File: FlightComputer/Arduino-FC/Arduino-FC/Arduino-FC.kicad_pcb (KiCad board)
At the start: 2 copper layers, 128.5 x 95.7 mm, 16 parts, among them J1 Conn_01x04, J2 Conn_01x08, J3 Conn_01x06, J4 Conn_01x03, J5 Conn_02x04_Odd_Even

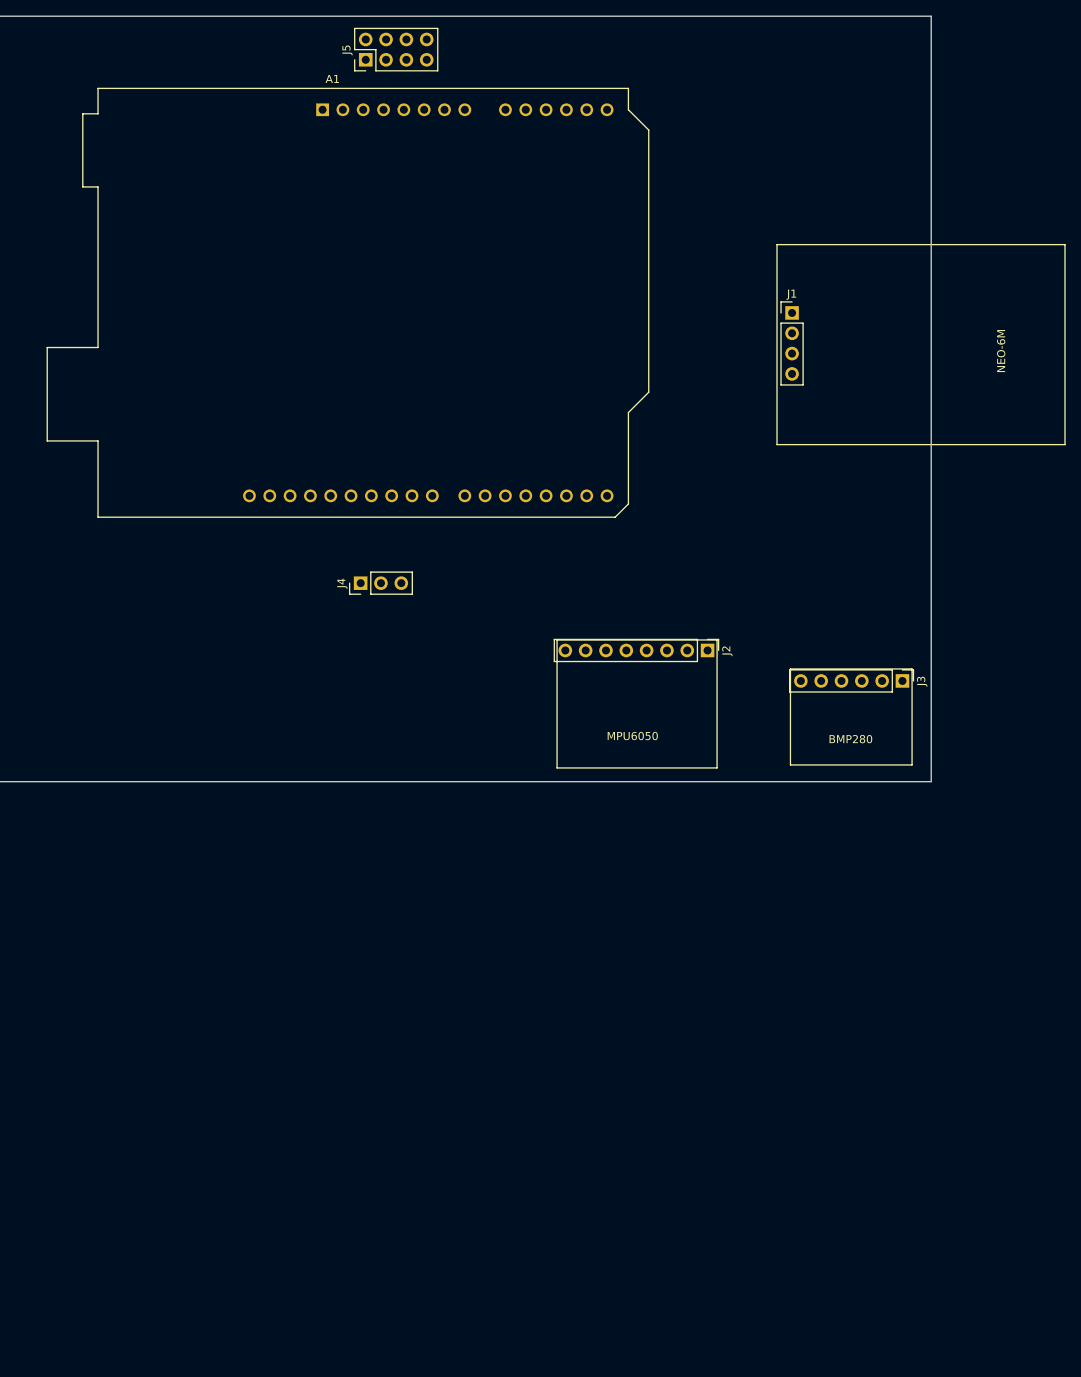
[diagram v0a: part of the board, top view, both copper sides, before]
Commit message: Custom NRF Adapter footprint
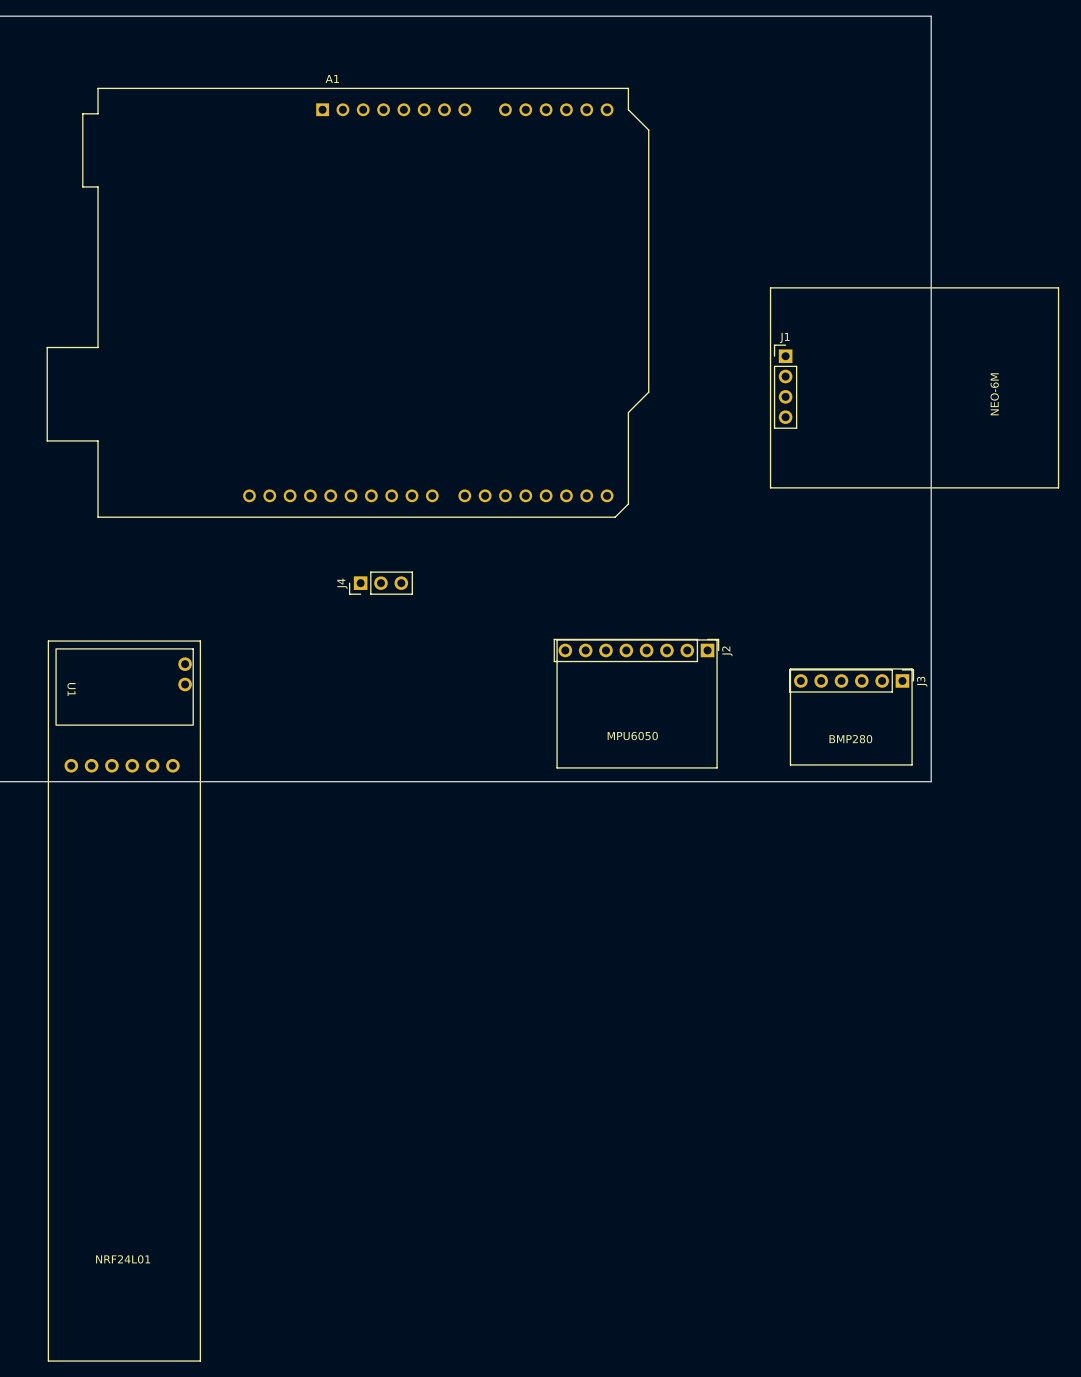
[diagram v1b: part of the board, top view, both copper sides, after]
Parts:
- removed J5: Conn_02x04_Odd_Even, Connector_PinHeader_2.54mm:PinHeader_2x04_P2.54mm_Vertical
- added U1: NRF24L01_Breakout, nRF24L01:nRF24L01-Adapter, F.Cu at (120.0, 133.3)
- moved J1 5.47 mm to (203.0, 84.7)
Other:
- board text added: "NRF24L01"

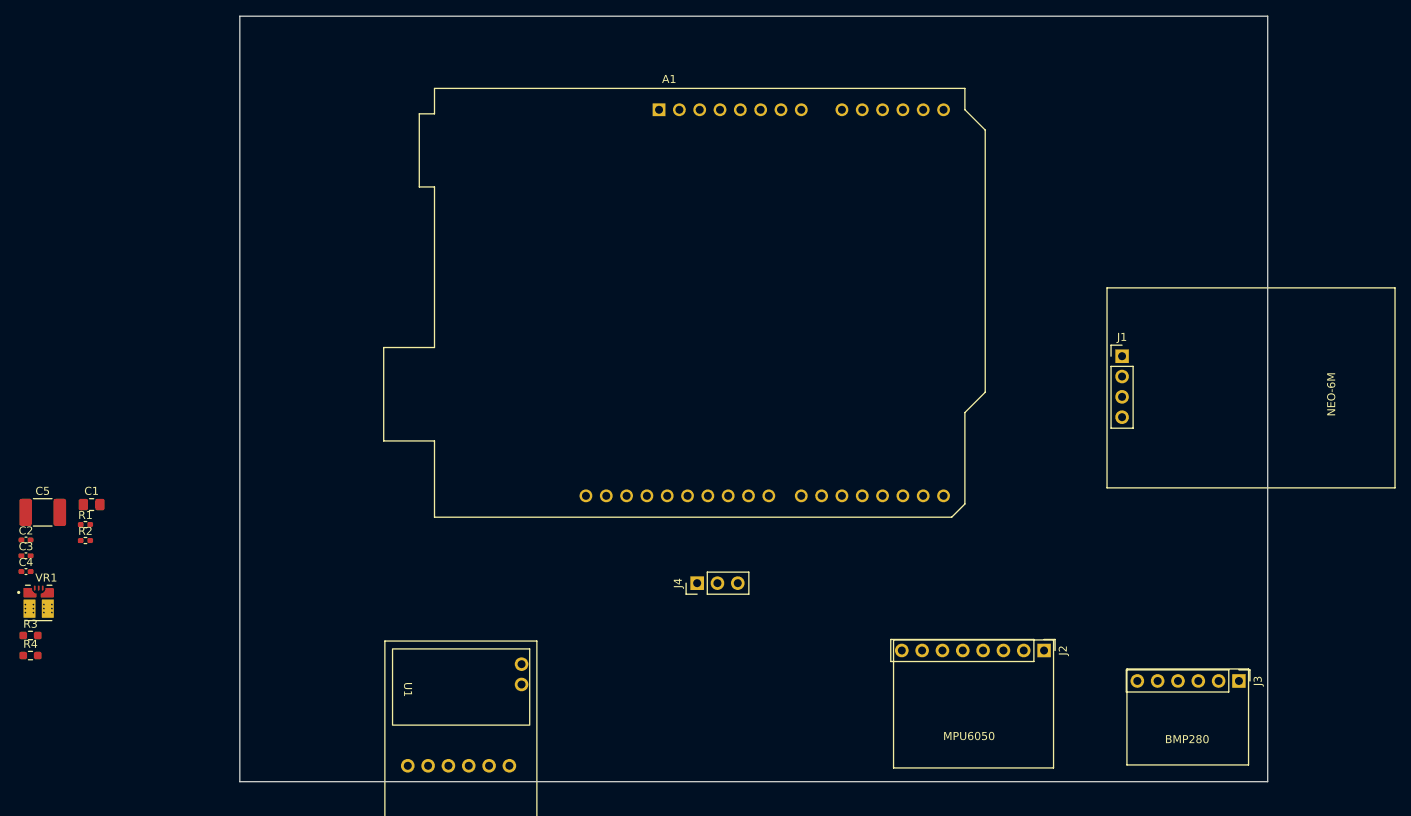
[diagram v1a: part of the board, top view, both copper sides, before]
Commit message: Indicator LEDs + Screw terminal
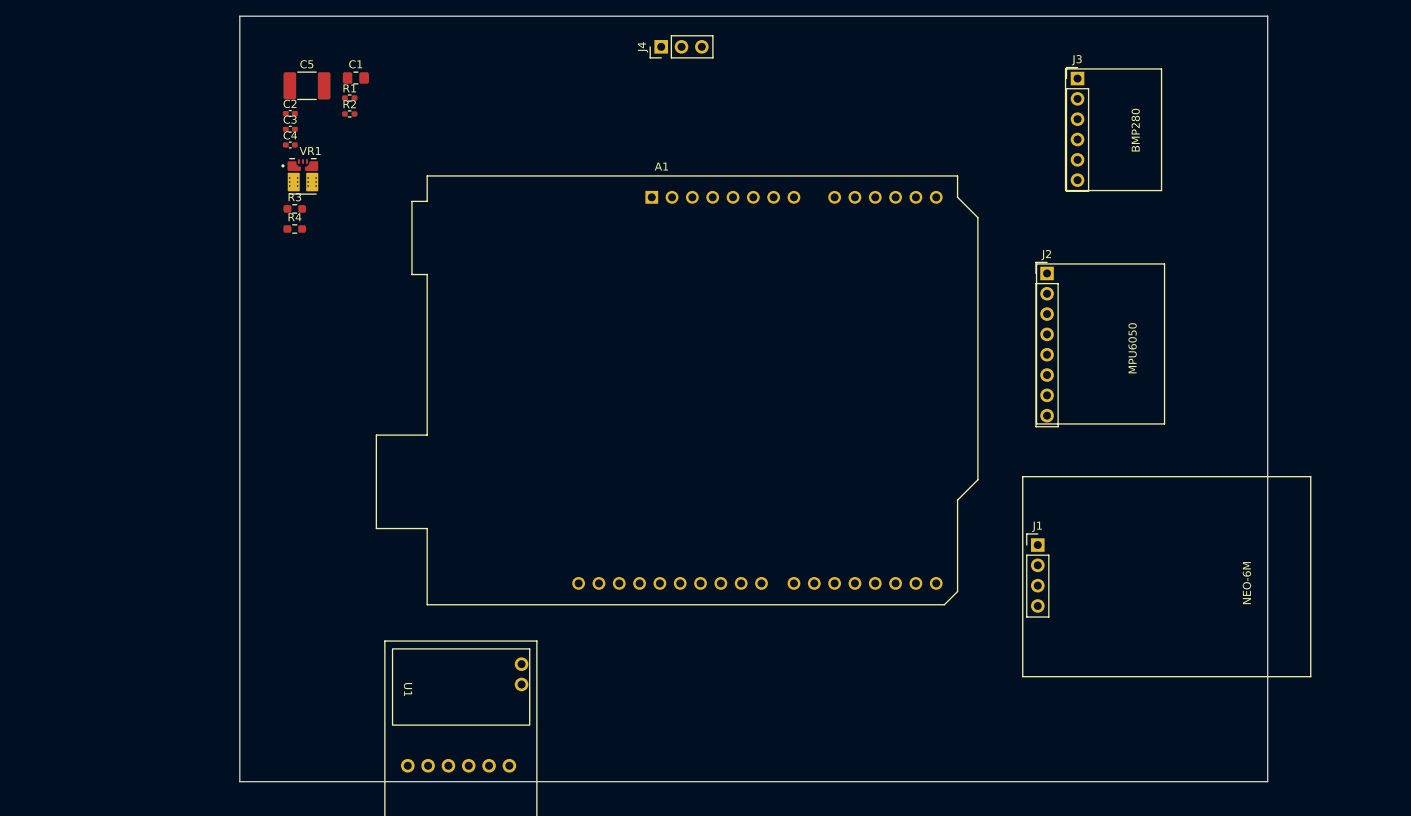
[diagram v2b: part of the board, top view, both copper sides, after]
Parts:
- moved J3 78.0 mm to (197.4, 50.0), turned to 0 degrees
- moved J4 67.2 mm to (145.4, 46.0)
- moved C1 62.7 mm to (107.2, 49.9)
- moved R3 62.7 mm to (99.6, 66.3)
- moved C5 62.7 mm to (101.1, 50.9)
- moved R1 62.7 mm to (106.4, 52.4)
- moved C2 62.7 mm to (99.0, 54.4)
- moved R2 62.7 mm to (106.4, 54.4)
- moved R4 62.7 mm to (99.6, 68.8)
- moved VR1 62.7 mm to (100.6, 62.3)
- moved C3 62.7 mm to (99.0, 56.3)
- moved C4 62.7 mm to (99.0, 58.3)
- moved J2 47.1 mm to (193.6, 74.3), turned to 0 degrees
- moved J1 25.8 mm to (192.5, 108.3)
- moved A1 11.0 mm to (144.2, 64.8)

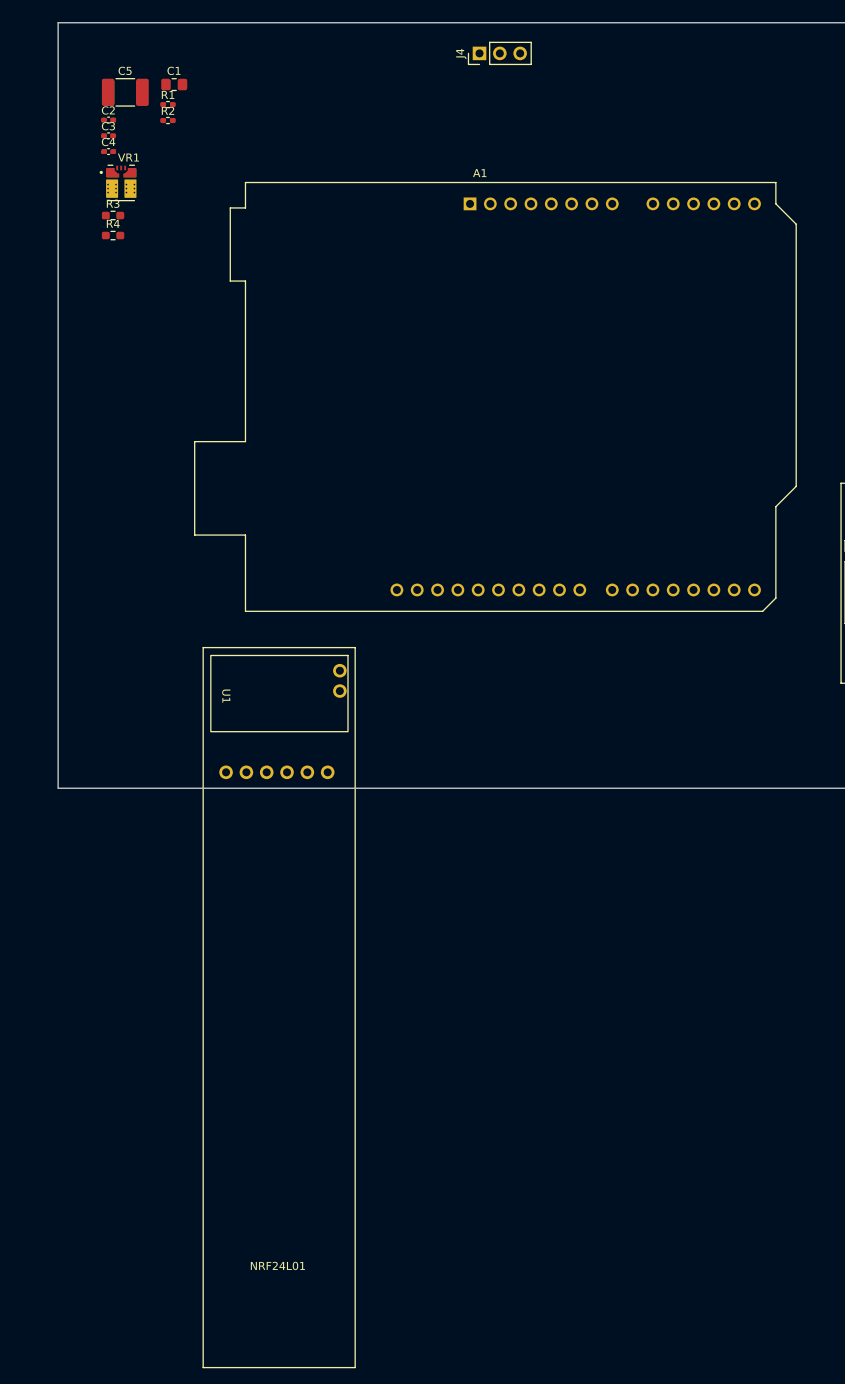
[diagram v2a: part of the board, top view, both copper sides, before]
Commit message: Added switch
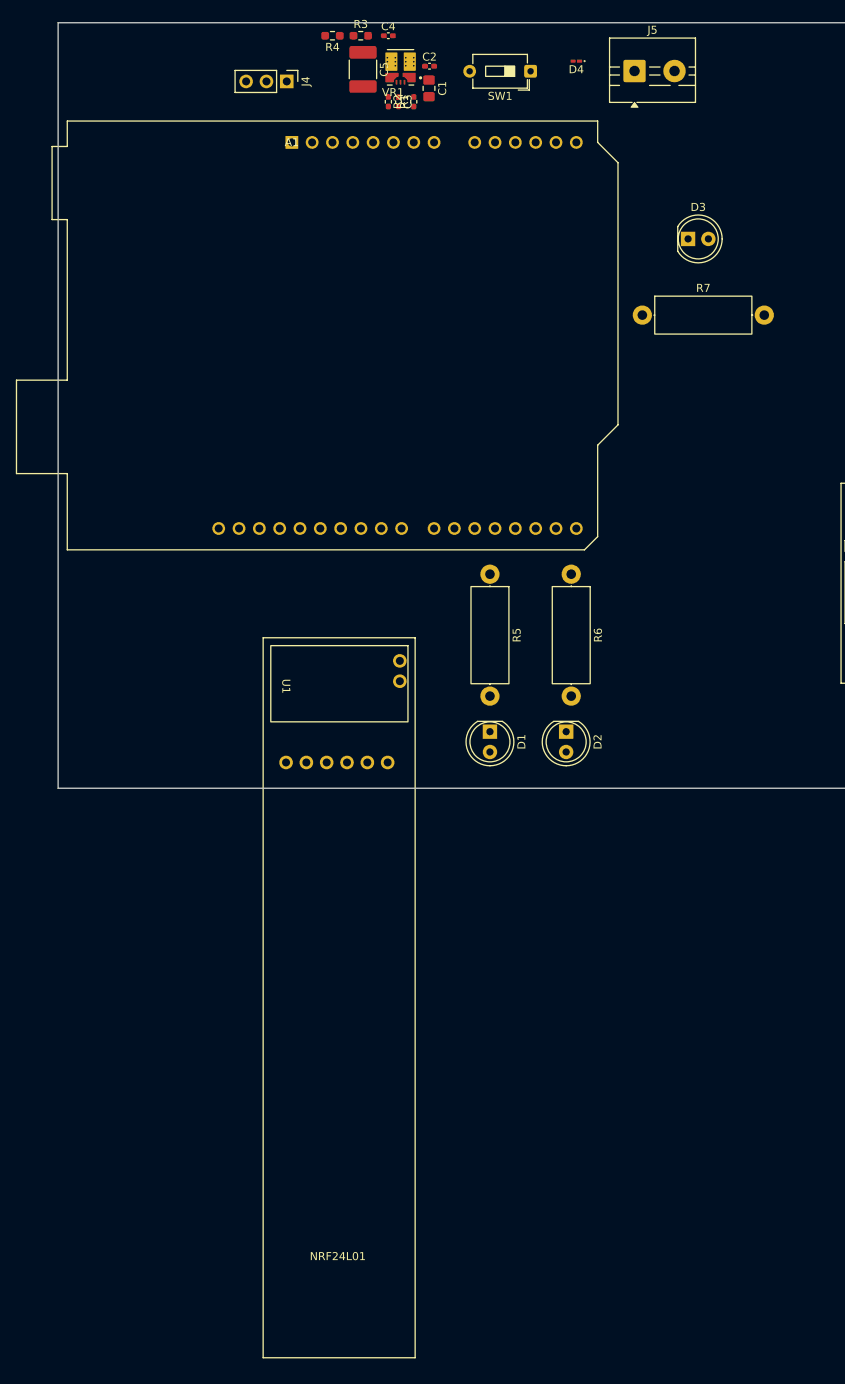
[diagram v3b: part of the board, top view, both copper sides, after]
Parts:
- added D1: LED, LED_THT:LED_D5.0mm_Clear, F.Cu at (146.7, 130.8)
- added D2: LED, LED_THT:LED_D5.0mm_Clear, F.Cu at (156.2, 130.8)
- added D3: LED, LED_THT:LED_D5.0mm_Clear, F.Cu at (171.4, 69.2)
- added D4: D_Schottky, Diode_SMD:D_0201_0603Metric_Pad0.64x0.40mm_HandSolder, F.Cu at (157.5, 47.0)
- added J5: Screw_Terminal_01x02, TerminalBlock:TerminalBlock_MaiXu_MX126-5.0-02P_1x02_P5.00mm, F.Cu at (164.8, 48.2)
- added R5: 470, Resistor_THT:R_Axial_DIN0414_L11.9mm_D4.5mm_P15.24mm_Horizontal, F.Cu at (146.7, 111.1)
- added R6: 470, Resistor_THT:R_Axial_DIN0414_L11.9mm_D4.5mm_P15.24mm_Horizontal, F.Cu at (156.8, 111.1)
- added R7: 1k, Resistor_THT:R_Axial_DIN0414_L11.9mm_D4.5mm_P15.24mm_Horizontal, F.Cu at (165.7, 78.7)
- added SW1: SW_SPST, Button_Switch_THT:SW_DIP_SPSTx01_Slide_6.7x4.1mm_W7.62mm_P2.54mm_LowProfile, F.Cu at (151.8, 48.3)
- moved C2 40.7 mm to (139.1, 47.6)
- moved R3 38.3 mm to (130.5, 43.8)
- moved C4 37.9 mm to (134.0, 43.8)
- moved VR1 37.8 mm to (135.5, 47.7), turned to 180 degrees
- moved R4 37.1 mm to (127.0, 43.8), turned to 180 degrees
- moved C3 36.5 mm to (135.3, 52.1), turned to -90 degrees
- moved C1 31.9 mm to (139.1, 50.4), turned to -90 degrees
- moved R1 30.7 mm to (137.2, 52.1), turned to 90 degrees
- moved C5 29.8 mm to (130.8, 48.0), turned to -90 degrees
- moved R2 27.6 mm to (134.0, 52.1), turned to -90 degrees
- moved J4 24.3 mm to (121.3, 49.5), turned to -90 degrees
- moved A1 23.6 mm to (121.9, 57.1)
- moved U1 7.60 mm to (127.5, 132.1)
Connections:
- A1 pad 20: unconnected-(A1-D5-Pad20) -> Net-(A1-D5)
- A1 pad 21: unconnected-(A1-D6-Pad21) -> Net-(A1-D6)

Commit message: Diode + Power Jumper
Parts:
- removed SW1: SW_SPST, Button_Switch_THT:SW_DIP_SPSTx01_Slide_6.7x4.1mm_W7.62mm_P2.54mm_LowProfile
- added J6: Conn_01x02, Connector_PinHeader_2.54mm:PinHeader_1x02_P2.54mm_Vertical, F.Cu at (147.2, 47.0)
- added J7: Conn_01x02, Connector_PinHeader_2.54mm:PinHeader_1x02_P2.54mm_Vertical, F.Cu at (176.5, 131.4)
- C2: footprint Capacitor_SMD:C_0402_1005Metric_Pad0.74x0.62mm_HandSolder -> Capacitor_SMD:C_0805_2012Metric_Pad1.18x1.45mm_HandSolder
- D4: footprint Diode_SMD:D_0201_0603Metric_Pad0.64x0.40mm_HandSolder -> SS34:DO-214AC
- R1: value 37.4K -> 28.7K
- moved J5 7.27 mm to (172.0, 47.6), turned to 180 degrees
